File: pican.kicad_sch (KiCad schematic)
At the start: 37 parts, among them J1 Uart, J2 Conn_01x04_MountingPin, J3 Raspberry_Pi_2_3, J4 Uart, Q1 FDD4243, U1 MCP2558FD-xSN, U2 MCP2515-xSO, U3 R-78B5.0-2.0, U4 LTC280X, Y1 16MHz

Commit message: board nearly finished
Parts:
- added TP2: GND, TestPoint:TestPoint_Keystone_5015_Micro-Minature, symbol Connector:TestPoint
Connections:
- net GND: now also TP2.1

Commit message: researched parts
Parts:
- C16: MOUSER_NO (none) -> 81-GRM155C80J224KE1D
- C17: MOUSER_NO (none) -> GCM21BR71H224K37L
- C18, C19: MOUSER_NO (none) -> 81-GCG21BR71E105MA2K
- C20: MOUSER_NO (none) -> 81-GRM18R61A105KA61J
- J1, J4: MOUSER_NO 538-502382-0670 -> 538-53047-0310
- J2: Farnell_NO (none) -> 9733060
- J3: MOUSER_NO 200-SSQ11001GD -> DO NOT ORDER
- JP1, TP1: MOUSER_NO (none) -> DO NOT ORDER
- L1: MOUSER_NO (none) -> 81-LQH2MCN100M52L
- TP2: MOUSER_NO (none) -> 534-5015
- U4: MOUSER_NO (none) -> 584-LTC2802CDE#PBF

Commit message: updated board with new connector
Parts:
- J2: footprint Connector_Molex:Molex_PicoBlade_53047-0410_1x04_P1.25mm_Vertical -> Connector_Molex:Molex_CLIK-Mate_502382-0470_1x04-1MP_P1.25mm_Vertical
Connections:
- net CAN_H: now also J2.2 (Pin_2); no longer J2.3 (Pin_3)
- net CAN_L: now also J2.3 (Pin_3); no longer J2.2 (Pin_2)
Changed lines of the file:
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@@
 (kicad_sch (version 20210621) (generator eeschema)
   (paper "A4")
-  (junction (at 179.705 28.575) (diameter 0.9144) (color 0 0 0 0))
-  (junction (at 174.625 28.575) (diameter 0.9144) (color 0 0 0 0))
-  (junction (at 30.48 163.195) (diameter 0.9144) (color 0 0 0 0))
-  (junction (at 97.79 172.085) (diameter 0.9144) (color 0 0 0 0))
-  (junction (at 247.65 155.575) (diameter 0) (color 0 0 0 0))
-  (junction (at 88.265 34.925) (diameter 0.9144) (color 0 0 0 0))
-  (junction (at 30.48 172.085) (diameter 0.9144) (color 0 0 0 0))
-  (junction (at 44.45 128.905) (diameter 0.9144) (color 0 0 0 0))
-  (junction (at 80.01 128.905) (diameter 0.9144) (color 0 0 0 0))
-  (junction (at 156.21 184.15) (diameter 0.9144) (color 0 0 0 0))
-  (junction (at 62.23 172.085) (diameter 0.9144) (color 0 0 0 0))
-  (junction (at 35.56 163.195) (diameter 0.9144) (color 0 0 0 0))
-  (junction (at 64.77 108.585) (diameter 0.9144) (color 0 0 0 0))
-  (junction (at 260.35 129.54) (diameter 0) (color 0 0 0 0))
-  (junction (at 250.19 129.54) (diameter 0) (color 0 0 0 0))
+  (junction (at 33.655 65.405) (diameter 0.9144) (color 0 0 0 0))
+  (junction (at 62.23 163.195) (diameter 0.9144) (color 0 0 0 0))
   (junction (at 31.115 53.975) (diameter 0.9144) (color 0 0 0 0))
-  (junction (at 177.165 97.155) (diameter 0.9144) (color 0 0 0 0))
-  (junction (at 78.74 172.085) (diameter 0.9144) (color 0 0 0 0))
+  (junction (at 75.565 34.925) (diameter 0.9144) (color 0 0 0 0))
+  (junction (at 164.465 97.155) (diameter 0.9144) (color 0 0 0 0))
+  (junction (at 23.495 62.865) (diameter 0.9144) (color 0 0 0 0))
+  (junction (at 216.535 132.08) (diameter 0) (color 0 0 0 0))
   (junction (at 77.47 112.395) (diameter 0.9144) (color 0 0 0 0))
+  (junction (at 174.625 97.155) (diameter 0.9144) (color 0 0 0 0))
   (junction (at 167.005 97.155) (diameter 0.9144) (color 0 0 0 0))
   (junction (at 207.01 118.11) (diameter 0) (color 0 0 0 0))
+  (junction (at 44.45 128.905) (diameter 0.9144) (color 0 0 0 0))
+  (junction (at 90.17 163.195) (diameter 0.9144) (color 0 0 0 0))
+  (junction (at 30.48 163.195) (diameter 0.9144) (color 0 0 0 0))
+  (junction (at 97.79 163.195) (diameter 0.9144) (color 0 0 0 0))
+  (junction (at 23.495 57.785) (diameter 0.9144) (color 0 0 0 0))
+  (junction (at 80.01 128.905) (diameter 0.9144) (color 0 0 0 0))
+  (junction (at 88.265 34.925) (diameter 0.9144) (color 0 0 0 0))
+  (junction (at 31.115 61.595) (diameter 0.9144) (color 0 0 0 0))
+  (junction (at 67.31 172.085) (diameter 0.9144) (color 0 0 0 0))
+  (junction (at 156.21 184.15) (diameter 0.9144) (color 0 0 0 0))
+  (junction (at 97.79 172.085) (diameter 0.9144) (color 0 0 0 0))
+  (junction (at 67.31 163.195) (diameter 0.9144) (color 0 0 0 0))
+  (junction (at 78.74 172.085) (diameter 0.9144) (color 0 0 0 0))
+  (junction (at 264.16 129.54) (diameter 0) (color 0 0 0 0))
+  (junction (at 169.545 97.155) (diameter 0.9144) (color 0 0 0 0))
+  (junction (at 35.56 172.085) (diameter 0.9144) (color 0 0 0 0))
+  (junction (at 177.165 97.155) (diameter 0.9144) (color 0 0 0 0))
+  (junction (at 64.77 108.585) (diameter 0.9144) (color 0 0 0 0))
+  (junction (at 250.19 129.54) (diameter 0) (color 0 0 0 0))
+  (junction (at 202.565 118.11) (diameter 0) (color 0 0 0 0))
+  (junction (at 75.565 31.115) (diameter 0.9144) (color 0 0 0 0))
+  (junction (at 57.15 163.195) (diameter 0.9144) (color 0 0 0 0))
   (junction (at 64.77 112.395) (diameter 0.9144) (color 0 0 0 0))
-  (junction (at 264.16 129.54) (diameter 0) (color 0 0 0 0))
-  (junction (at 174.625 97.155) (diameter 0.9144) (color 0 0 0 0))
-  (junction (at 31.115 61.595) (diameter 0.9144) (color 0 0 0 0))
-  (junction (at 90.17 163.195) (diameter 0.9144) (color 0 0 0 0))
-  (junction (at 35.56 172.085) (diameter 0.9144) (color 0 0 0 0))
-  (junction (at 33.655 65.405) (diameter 0.9144) (color 0 0 0 0))
+  (junction (at 62.23 172.085) (diameter 0.9144) (color 0 0 0 0))
+  (junction (at 80.01 123.825) (diameter 0.9144) (color 0 0 0 0))
   (junction (at 177.165 28.575) (diameter 0.9144) (color 0 0 0 0))
+  (junction (at 52.07 137.795) (diameter 0.9144) (color 0 0 0 0))
+  (junction (at 172.085 97.155) (diameter 0.9144) (color 0 0 0 0))
+  (junction (at 90.17 172.085) (diameter 0.9144) (color 0 0 0 0))
+  (junction (at 107.95 163.195) (diameter 0.9144) (color 0 0 0 0))
+  (junction (at 174.625 28.575) (diameter 0.9144) (color 0 0 0 0))
+  (junction (at 148.59 184.15) (diameter 0.9144) (color 0 0 0 0))
+  (junction (at 179.705 28.575) (diameter 0.9144) (color 0 0 0 0))
+  (junction (at 247.65 155.575) (diameter 0) (color 0 0 0 0))
+  (junction (at 35.56 163.195) (diameter 0.9144) (color 0 0 0 0))
+  (junction (at 24.13 163.195) (diameter 0.9144) (color 0 0 0 0))
+  (junction (at 64.77 137.795) (diameter 0.9144) (color 0 0 0 0))
+  (junction (at 30.48 172.085) (diameter 0.9144) (color 0 0 0 0))
   (junction (at 167.005 28.575) (diameter 0.9144) (color 0 0 0 0))
-  (junction (at 67.31 163.195) (diameter 0.9144) (color 0 0 0 0))
-  (junction (at 23.495 57.785) (diameter 0.9144) (color 0 0 0 0))
-  (junction (at 23.495 62.865) (diameter 0.9144) (color 0 0 0 0))
-  (junction (at 52.07 137.795) (diameter 0.9144) (color 0 0 0 0))
-  (junction (at 24.13 163.195) (diameter 0.9144) (color 0 0 0 0))
-  (junction (at 90.17 172.085) (diameter 0.9144) (color 0 0 0 0))
-  (junction (at 67.31 172.085) (diameter 0.9144) (color 0 0 0 0))
   (junction (at 45.72 172.085) (diameter 0.9144) (color 0 0 0 0))
-  (junction (at 164.465 97.155) (diameter 0.9144) (color 0 0 0 0))
-  (junction (at 57.15 163.195) (diameter 0.9144) (color 0 0 0 0))
-  (junction (at 172.085 97.155) (diameter 0.9144) (color 0 0 0 0))
-  (junction (at 97.79 163.195) (diameter 0.9144) (color 0 0 0 0))
-  (junction (at 202.565 118.11) (diameter 0) (color 0 0 0 0))
-  (junction (at 62.23 163.195) (diameter 0.9144) (color 0 0 0 0))
-  (junction (at 64.77 137.795) (diameter 0.9144) (color 0 0 0 0))
-  (junction (at 107.95 163.195) (diameter 0.9144) (color 0 0 0 0))
-  (junction (at 80.01 123.825) (diameter 0.9144) (color 0 0 0 0))
-  (junction (at 169.545 97.155) (diameter 0.9144) (color 0 0 0 0))
-  (junction (at 75.565 31.115) (diameter 0.9144) (color 0 0 0 0))
-  (junction (at 216.535 132.08) (diameter 0) (color 0 0 0 0))
-  (junction (at 75.565 34.925) (diameter 0.9144) (color 0 0 0 0))
-  (junction (at 148.59 184.15) (diameter 0.9144) (color 0 0 0 0))
+  (junction (at 260.35 129.54) (diameter 0) (color 0 0 0 0))
   (no_connect (at 151.765 60.325))
   (no_connect (at 151.765 57.785))
@@
     (stroke (width 0) (type solid) (color 0 0 0 0))
   )
+  (wire (pts (xy 250.19 129.54) (xy 252.095 129.54))
+    (stroke (width 0) (type default) (color 0 0 0 0))
+  )
   (wire (pts (xy 238.76 129.54) (xy 250.19 129.54))
     (stroke (width 0) (type default) (color 0 0 0 0))
   )
-  (wire (pts (xy 250.19 129.54) (xy 252.095 129.54))
-    (stroke (width 0) (type default) (color 0 0 0 0))
-  )
   (wire (pts (xy 45.72 168.275) (xy 45.72 172.085))
     (stroke (width 0) (type solid) (color 0 0 0 0))
@@
     (stroke (width 0) (type solid) (color 0 0 0 0))
   )
+  (wire (pts (xy 260.35 134.62) (xy 260.35 129.54))
+    (stroke (width 0) (type default) (color 0 0 0 0))
+  )
   (wire (pts (xy 238.76 134.62) (xy 260.35 134.62))
     (stroke (width 0) (type default) (color 0 0 0 0))
   )
-  (wire (pts (xy 260.35 134.62) (xy 260.35 129.54))
-    (stroke (width 0) (type default) (color 0 0 0 0))
-  )
   (wire (pts (xy 174.625 29.845) (xy 174.625 28.575))
     (stroke (width 0) (type solid) (color 0 0 0 0))
@@
     (stroke (width 0) (type default) (color 0 0 0 0))
   )
+  (wire (pts (xy 219.71 133.35) (xy 216.535 133.35))
+    (stroke (width 0) (type default) (color 0 0 0 0))
+  )
+  (wire (pts (xy 216.535 132.08) (xy 216.535 133.35))
+    (stroke (width 0) (type default) (color 0 0 0 0))
+  )
   (wire (pts (xy 216.535 130.81) (xy 216.535 132.08))
     (stroke (width 0) (type default) (color 0 0 0 0))
   )
-  (wire (pts (xy 216.535 132.08) (xy 216.535 133.35))
-    (stroke (width 0) (type default) (color 0 0 0 0))
-  )
-  (wire (pts (xy 219.71 133.35) (xy 216.535 133.35))
-    (stroke (width 0) (type default) (color 0 0 0 0))
-  )
   (wire (pts (xy 148.59 184.15) (xy 156.21 184.15))
     (stroke (width 0) (type solid) (color 0 0 0 0))
@@
     (stroke (width 0) (type default) (color 0 0 0 0))
   )
+  (wire (pts (xy 241.3 155.575) (xy 247.65 155.575))
+    (stroke (width 0) (type default) (color 0 0 0 0))
+  )
   (wire (pts (xy 238.76 142.24) (xy 241.3 142.24))
-    (stroke (width 0) (type default) (color 0 0 0 0))
-  )
-  (wire (pts (xy 241.3 155.575) (xy 247.65 155.575))
     (stroke (width 0) (type default) (color 0 0 0 0))
   )
@@
     (effects (font (size 1.27 1.27)) (justify right bottom))
   )
-  (label "CAN_L" (at 157.48 180.34 180)
+  (label "CAN_L" (at 157.48 177.8 180)
     (effects (font (size 1.27 1.27)) (justify right bottom))
   )
@@
     (effects (font (size 1.27 1.27)) (justify right bottom))
   )
-  (label "CAN_H" (at 157.48 177.8 180)
+  (label "CAN_H" (at 157.48 180.34 180)
     (effects (font (size 1.27 1.27)) (justify right bottom))
   )
@@
       (effects (font (size 1.27 1.27)) (justify left))
     )
-    (property "Footprint" "Connector_Molex:Molex_PicoBlade_53047-0410_1x04_P1.25mm_Vertical" (id 2) (at 162.56 180.34 0)
+    (property "Footprint" "Connector_Molex:Molex_CLIK-Mate_502382-0470_1x04-1MP_P1.25mm_Vertical" (id 2) (at 162.56 180.34 0)
       (effects (font (size 1.27 1.27)) hide)
     )
@@
     )
     (path "/d78664a7-b311-45df-8907-ff116b2d919c"
-      (reference "J2") (unit 1) (value "Conn_01x04_MountingPin") (footprint "Connector_Molex:Molex_PicoBlade_53047-0410_1x04_P1.25mm_Vertical")
+      (reference "J2") (unit 1) (value "Conn_01x04_MountingPin") (footprint "Connector_Molex:Molex_CLIK-Mate_502382-0470_1x04-1MP_P1.25mm_Vertical")
     )
     (path "/f654bc6c-28d4-4b93-aead-b7475c0c3c85"

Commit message: some stuff!
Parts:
- removed R2: 10k, Resistor_SMD:R_0603_1608Metric, symbol Device:R_Small
- removed U1: MCP2558FD-xSN, Package_SO:SOIC-8_3.9x4.9mm_P1.27mm, symbol Interface_CAN_LIN:MCP2558FD-xSN
- removed U2: MCP2515-xSO, Package_SO:SOIC-18W_7.5x11.6mm_P1.27mm, symbol Interface_CAN_LIN:MCP2515-xSO
- added U2: MCP2562FD-E-SN, Package_SO:SOIC-8_3.9x4.9mm_P1.27mm, symbol Interface_CAN_LIN:MCP2562-H-SN
- added U3: MCP2518FD-xSL, Package_SO:SOIC-14_3.9x8.7mm_P1.27mm, symbol Interface_CAN_LIN:MCP2517FD-xSL
- renumbered C13 to C11, C11 to C12, C12 to C13, C3 to C2, C4 to C3, C2 to C4, U3 to U1
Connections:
- net +3V3: now also U2.5 (Vio), U3.14 (VDD)
- net +5V: now also U2.3 (VDD)
- net CAN_H: now also U2.7 (CANH)
- net CAN_L: now also U2.6 (CANL)
- net CAN_RX: now also U2.4 (RXD), U3.2 (RXCAN)
- net CAN_TX: now also U2.1 (TXD), U3.1 (TXCAN)
- net GND: now also U2.2 (VSS), U2.8 (STBY), U3.7 (VSS)
- net INT: now also U3.4 (~{INT})
- net SPI_CE0: now also U3.13 (nCS)
- net SPI_MISO: now also U3.12 (SDO)
- net SPI_MOSI: now also U3.11 (SDI)
- net SPI_SCLK: now also U3.10 (SCK)
- no-connect marks 25 -> 23
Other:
- moved on the sheet: C10, C12, C13, C2, C3, C6, C9, D1, R1, Y1

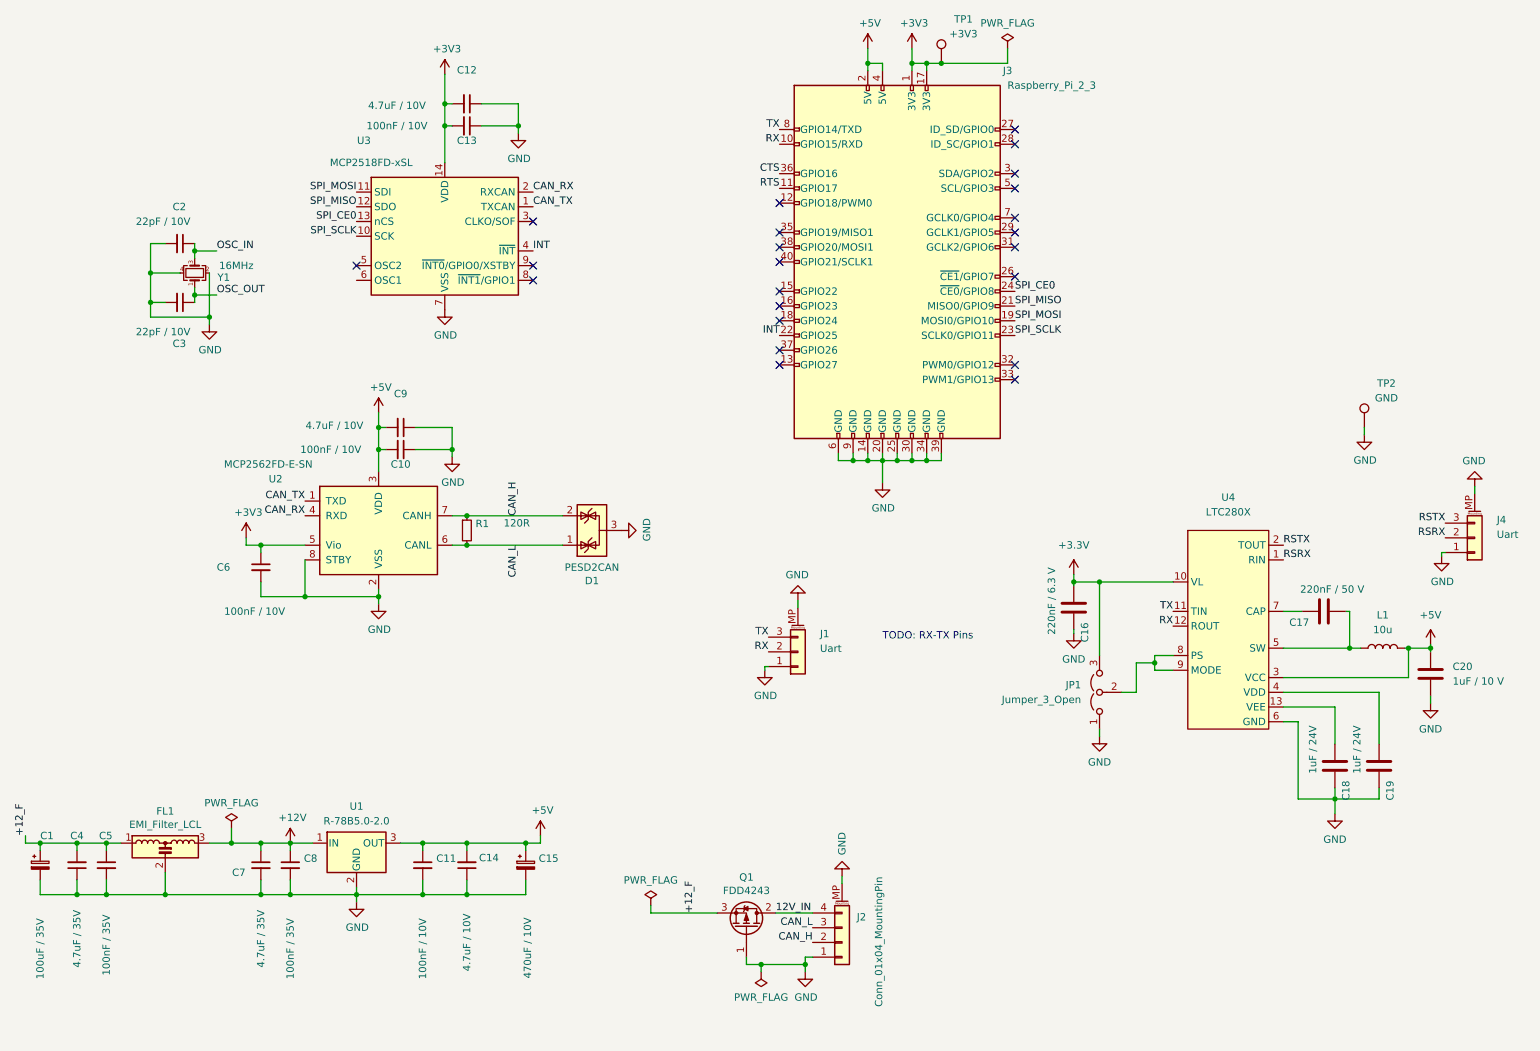
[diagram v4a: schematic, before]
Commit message: changed crystal to osc
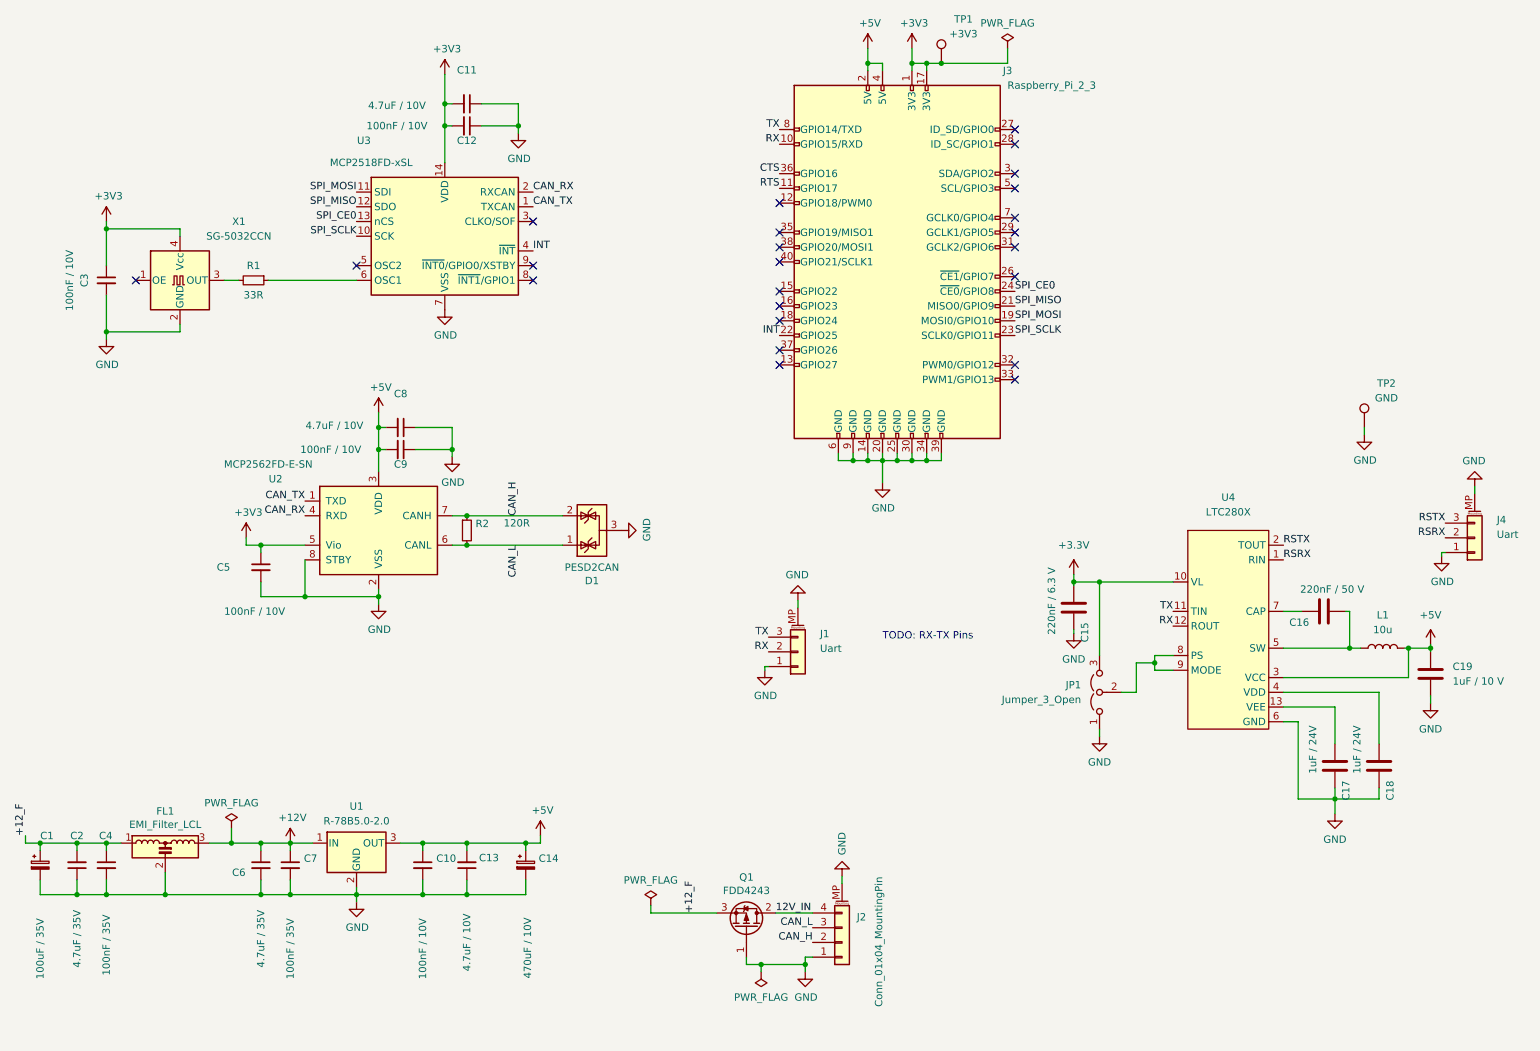
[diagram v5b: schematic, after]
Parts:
- removed C2: 22pF / 10V, Capacitor_SMD:C_0603_1608Metric, symbol Device:C_Small
- removed Y1: 16MHz, ownLib:Crystal_SMD_Abracon_ABM3B-4Pin_5.0x3.2mm, symbol Device:Crystal_GND24_Small
- added R1: 33R, Resistor_SMD:R_0402_1005Metric, symbol Device:R_Small
- added X1: SG-5032CCN, Oscillator:Oscillator_SMD_SeikoEpson_SG8002LB-4Pin_5.0x3.2mm, symbol Oscillator:SG-5032CCN
- C3: value 22pF / 10V -> 100nF / 10V; MOUSER_NO 77-VJ0603A220JXACBC -> 810-C1005X7R1H104K
- renumbered C11 to C10, C12 to C11, C13 to C12, C14 to C13, C15 to C14, C16 to C15, C17 to C16, C18 to C17, C19 to C18, C20 to C19, C4 to C2, C5 to C4, C6 to C5, C7 to C6, C8 to C7, C9 to C8, C10 to C9, R1 to R2
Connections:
- net OSC_OUT is gone; now on net +3V3: C3.1
- net +3V3: now also X1.4 (Vcc)
- net GND: now also X1.2 (GND)
- net at U3.6 (OSC1): now also R1.1
- new net: R1.2, X1.3 (OUT)
- no-connect marks 23 -> 24
